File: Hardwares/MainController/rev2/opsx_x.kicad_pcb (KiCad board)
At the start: 2 copper layers, 95.9 x 27.8 mm, 62 parts, among them J1 Conn_01x02, J3 Conn_01x02, Q1 Q_NMOS_GSD, Q2 Q_NMOS_GSD, Q3 Q_PMOS_GSD, Q4 MMBT3904, U1 RP2040, U2 TLV70433DBVR, U3 W25Q128JVS, U4 OPTICAL-TSL2561T(6P-3.8X2.6MM)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

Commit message: 声纳工作正常
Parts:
- removed D6: LED, Diode_SMD:D_0603_1608Metric_Pad1.05x0.95mm_HandSolder
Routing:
- net /LED2: track 26.1 -> 0.00 mm, vias 2 -> 0
- net GND: track 71.8 -> 73.8 mm, vias 66 -> 95
- net /LED1: track 23.6 -> 21.8 mm
- net Net-(Q3-G): track 22.8 -> 21.6 mm
- net /S1F_PF_MCU: track 58.7 -> 58.1 mm
- net /GTD-3: track 10.8 -> 10.2 mm
- net /SDA1: track 7.42 -> 7.76 mm, vias 1 -> 2
- net /SCL1: track 7.08 -> 7.06 mm, vias 1 -> 2
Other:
- board text added: "SX-70 MK2 Rev2 by LZS"
- board text added: "UD+ UD-"
- board text removed: "OPSX-70 Rev2 by LZS"
- board text removed: "locked"

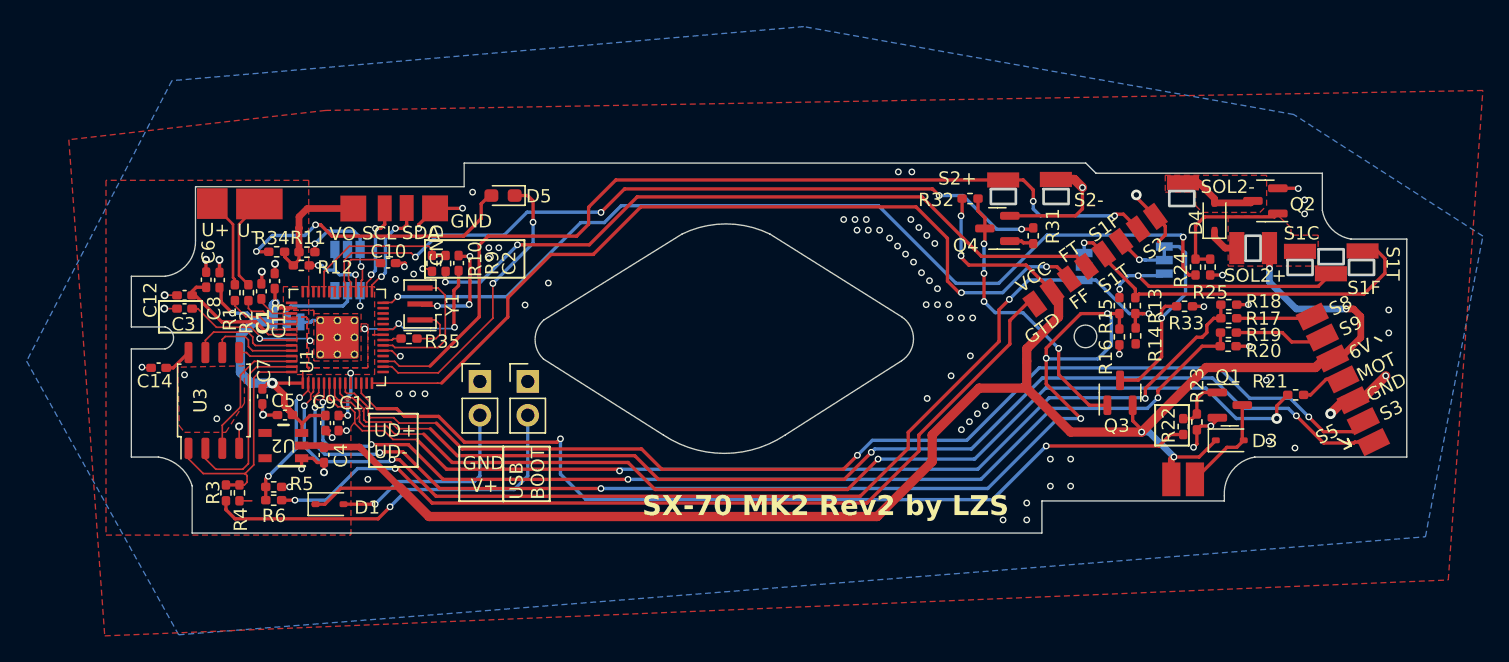
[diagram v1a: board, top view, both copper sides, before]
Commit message: 增加防抖，防止机身动作不到位
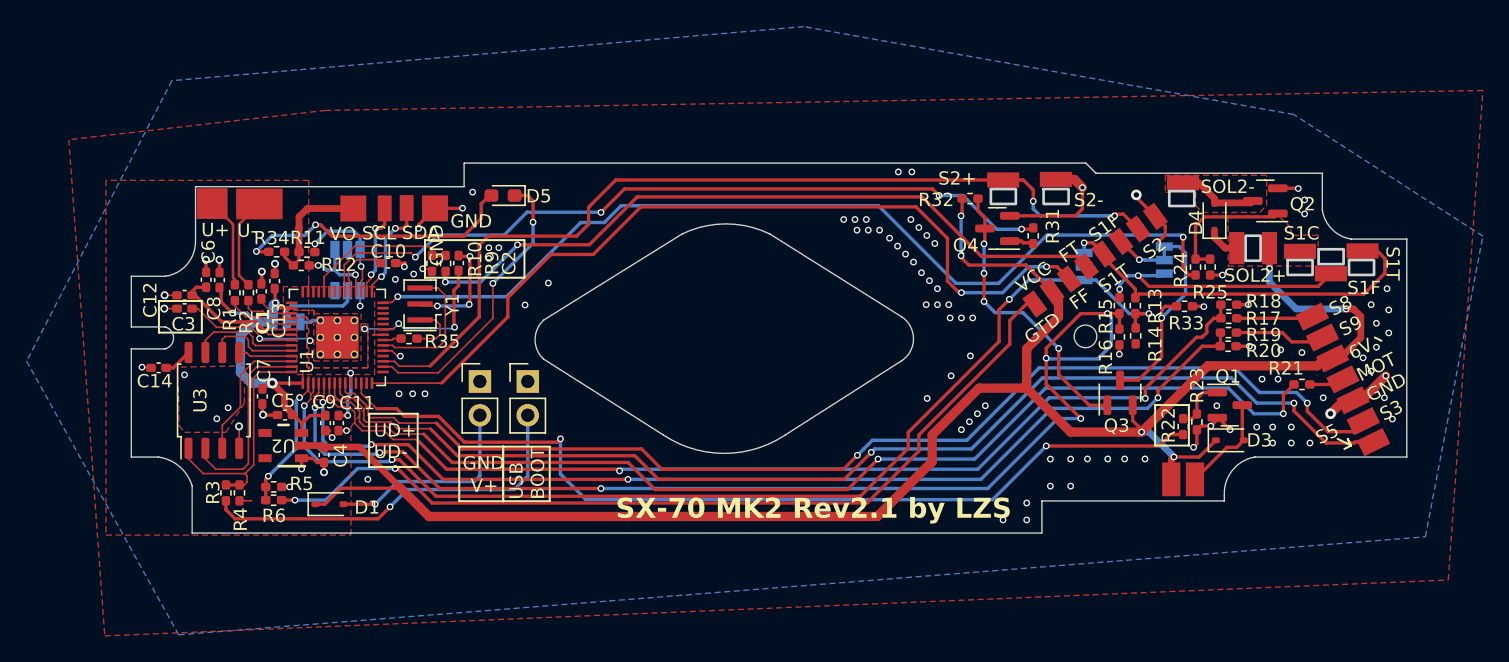
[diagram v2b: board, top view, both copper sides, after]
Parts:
- moved R21 0.92 mm to (113.4, 74.4)
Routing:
- net GND: track 73.8 -> 75.2 mm, vias 95 -> 117
- net /MOTOR: track 3.44 -> 2.64 mm
- net Net-(U1-GPIO5): track 81.4 -> 82.2 mm
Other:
- board text added: "SX-70 MK2 Rev2.1 by LZS"
- board text removed: "SX-70 MK2 Rev2 by LZS"
